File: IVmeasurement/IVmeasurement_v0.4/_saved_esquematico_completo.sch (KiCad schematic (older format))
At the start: 23 parts, among them Q1 IRF540N

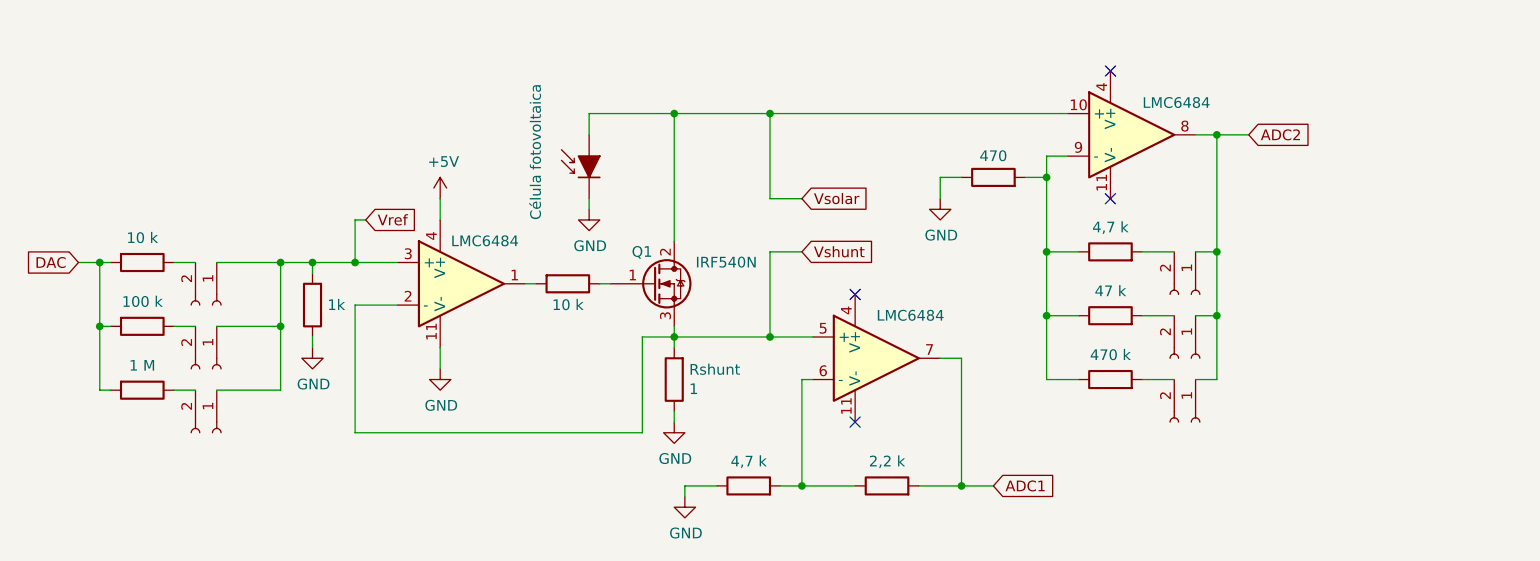
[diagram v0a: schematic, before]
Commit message: Low voltage DC-DC (MP3414 and bq25504)
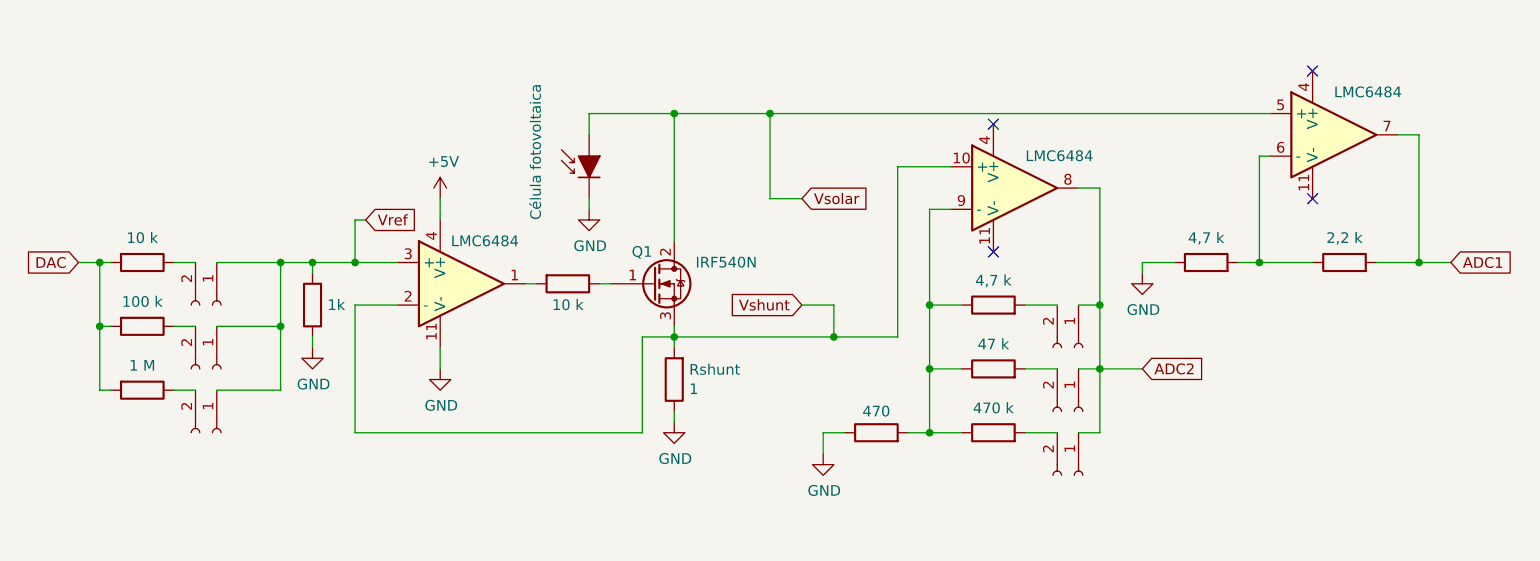
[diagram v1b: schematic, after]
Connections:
- net Vshunt: now also U?.10 (+); no longer U?.5 (+)
- net Vsolar: now also U?.5 (+); no longer U?.10 (+)
